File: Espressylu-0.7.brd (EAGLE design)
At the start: 101.6 x 76.2 mm, 135 parts, among them J1 4P-TERM-BLOCK284391-4, J10 M02POLAR, J11 M02POLAR, J2 M02POLAR, J3 M02POLAR, J4 M02POLAR, J5 HOTEND-1, J6 2x7, J7 HOTBED, J8 MICROSD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

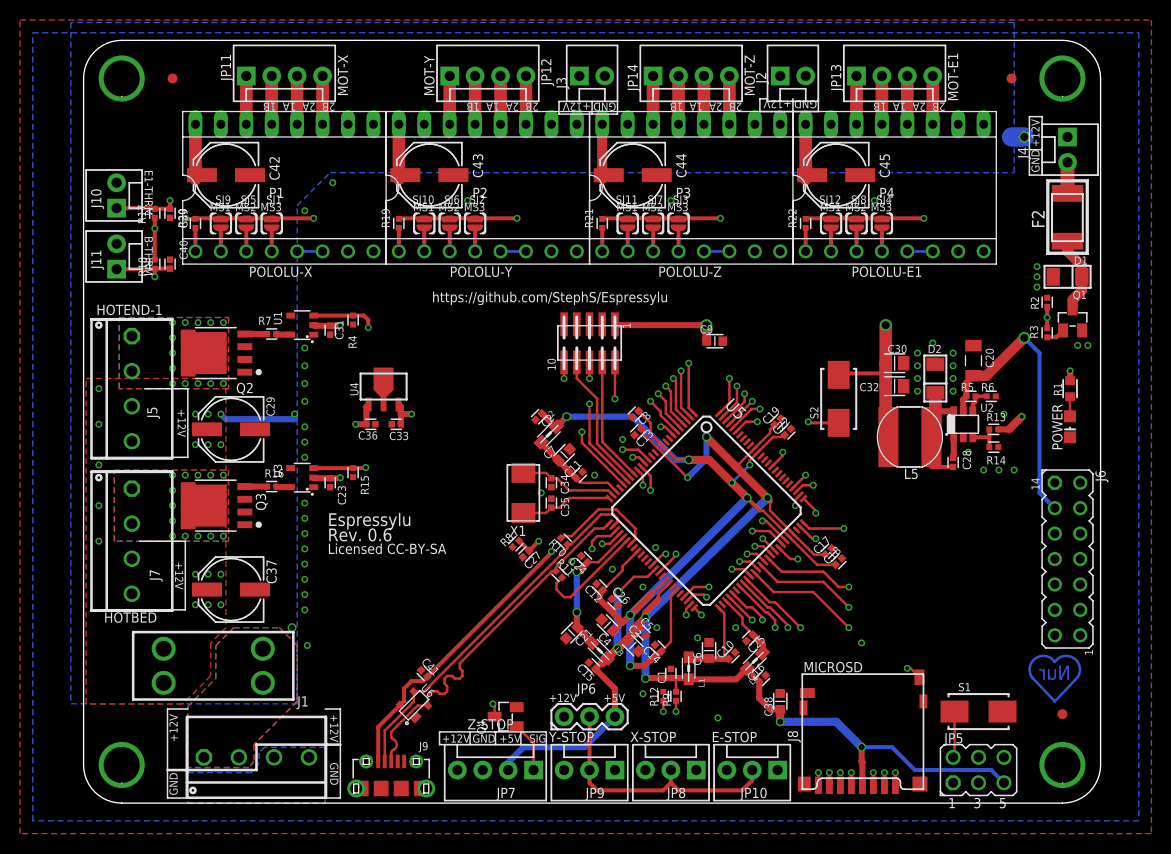
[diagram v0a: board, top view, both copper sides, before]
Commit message: Cleaned up Silkscreen and added caps
I cleaned up the silkscreen for all of the components.
Capacitors were added to the motor driver VCC pins.
More GND Vias were added to reduce noise.
The mosfets were shifted away from the connectors slightly.
The stepper motor connectors were shifted slightly closer to the edge of
the board.
All of the HV pins are labelled as 24v. This board should only be used
with 24v.
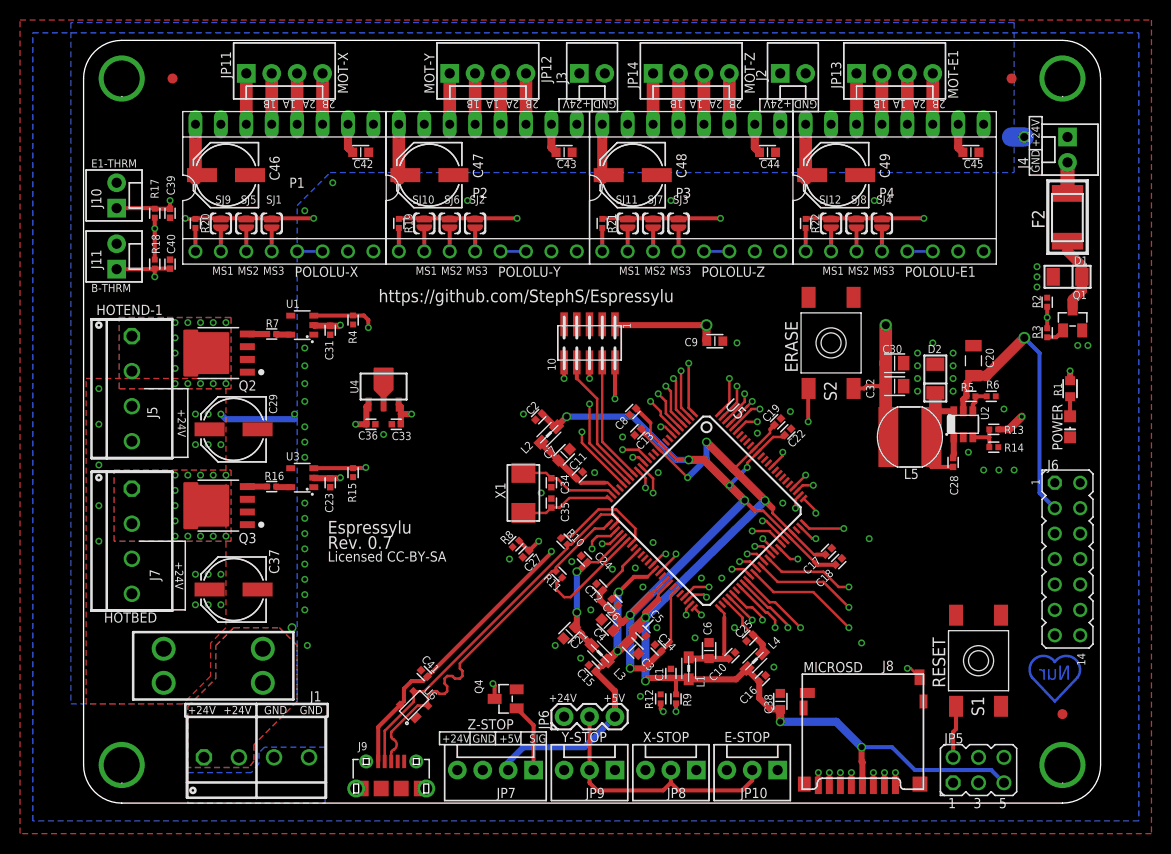
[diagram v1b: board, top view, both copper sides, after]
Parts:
- added C46, C47, C48, C49: 100uF, teensylu:PANASONIC_D
- C42, C43, C44, C45: value 100uF -> 4.7uF; device teensylu:PANASONIC_D -> teensylu:CAPC1608X92N
- S1: value (none) -> RESET; device teensylu:TACTILE_SWITCH_2P_SMD -> teensylu:SWITCH-SMD-4P
- S2: value (none) -> ERASE; device teensylu:TACTILE_SWITCH_2P_SMD -> teensylu:SWITCH-SMD-4P
- moved C43 13.7 mm to (48.0, 65.0)
- moved C45 13.7 mm to (88.6, 65.0)
- moved C42 13.7 mm to (27.7, 65.0)
- moved C44 13.7 mm to (68.3, 65.0)
- moved S2 5.64 mm to (74.7, 46.0)
- moved S1 5.08 mm to (89.4, 14.2), turned to 90 degrees
- moved Q4 1.78 mm to (42.2, 10.4)
- moved C8 0.36 mm to (54.9, 39.1)
- moved R12 0.36 mm to (57.7, 10.4)
- moved C29 0.25 mm to (15.0, 37.3)
- moved C37 0.25 mm to (15.0, 21.3)
- moved C15 0.25 mm to (50.8, 13.5)
- moved C3 0.25 mm to (54.9, 15.5)
- moved L3 0.25 mm to (51.6, 15.0)
- moved Q2 0.25 mm to (13.5, 45.0)
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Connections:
- net +3V3: now also C42.2, C43.2, C44.2, C45.2, S2.3; no longer S2.2
- net 24V: now also C46.+, C47.+, C48.+, C49.+; no longer C42.+, C43.+, C44.+, C45.+
- net GND: now also C42.1, C43.1, C44.1, C45.1, C46.-, C47.-, C48.-, C49.-, S1.3, S1.4; no longer C42.-, C43.-, C44.-, C45.-, S1.2
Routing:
- net +3V3: track 421.0 -> 431.9 mm
- net Z-STOP-BIAS: track 5.09 -> 6.86 mm
- net Z-STOP: track 31.1 -> 29.5 mm
- net VDD: track 100.6 -> 101.4 mm
- net !RESET: track 73.1 -> 73.7 mm
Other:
- board text added: "+24V"
- board text added: "Rev. 0.7"
- board text removed: "+12V"
- board text removed: "Rev. 0.6"
